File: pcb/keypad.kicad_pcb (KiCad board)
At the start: 2 copper layers, 53 x 53 mm, 36 parts, among them SW1 KS33_SW_solder, SW2 KS33_SW_solder, SW3 KS33_SW_solder, SW4 KS33_SW_solder, SW5 KS33_SW_solder, SW6 KS33_SW_solder, SW7 KS33_SW_solder, SW8 KS33_SW_solder, SW9 KS33_SW_solder, U1 74AHCT1G125, U2 XIAO-ESP32-C6-DIP

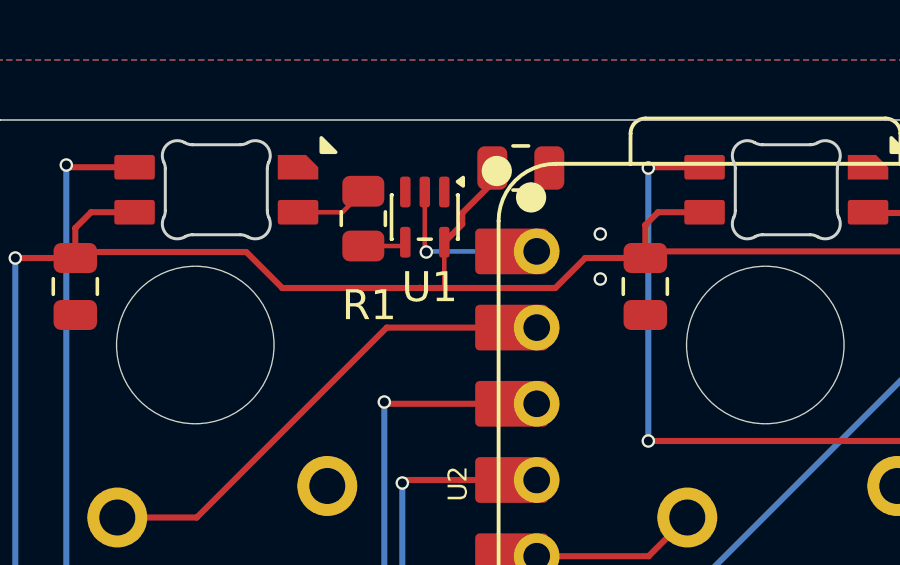
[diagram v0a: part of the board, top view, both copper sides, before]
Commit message: Swap U1 level shifter to SN74AHCT1G125DBVR (SOT-23-5)
The SOT-353 part was hard to hand solder. Same 74AHCT1G125 pinout, so only
the footprint changes. U1 shifts 0.1 mm right and its traces are rerouted;
gerbers regenerated.
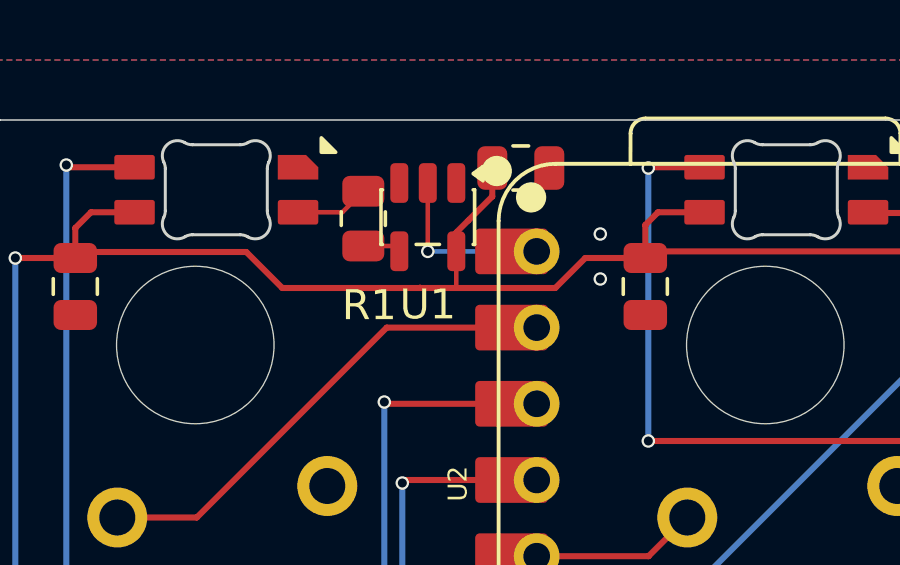
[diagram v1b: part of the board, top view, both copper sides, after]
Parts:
- U1: footprint Package_TO_SOT_SMD:SOT-353_SC-70-5 -> Package_TO_SOT_SMD:SOT-23-5
- moved U1 0.10 mm to (140.8, 78.7)

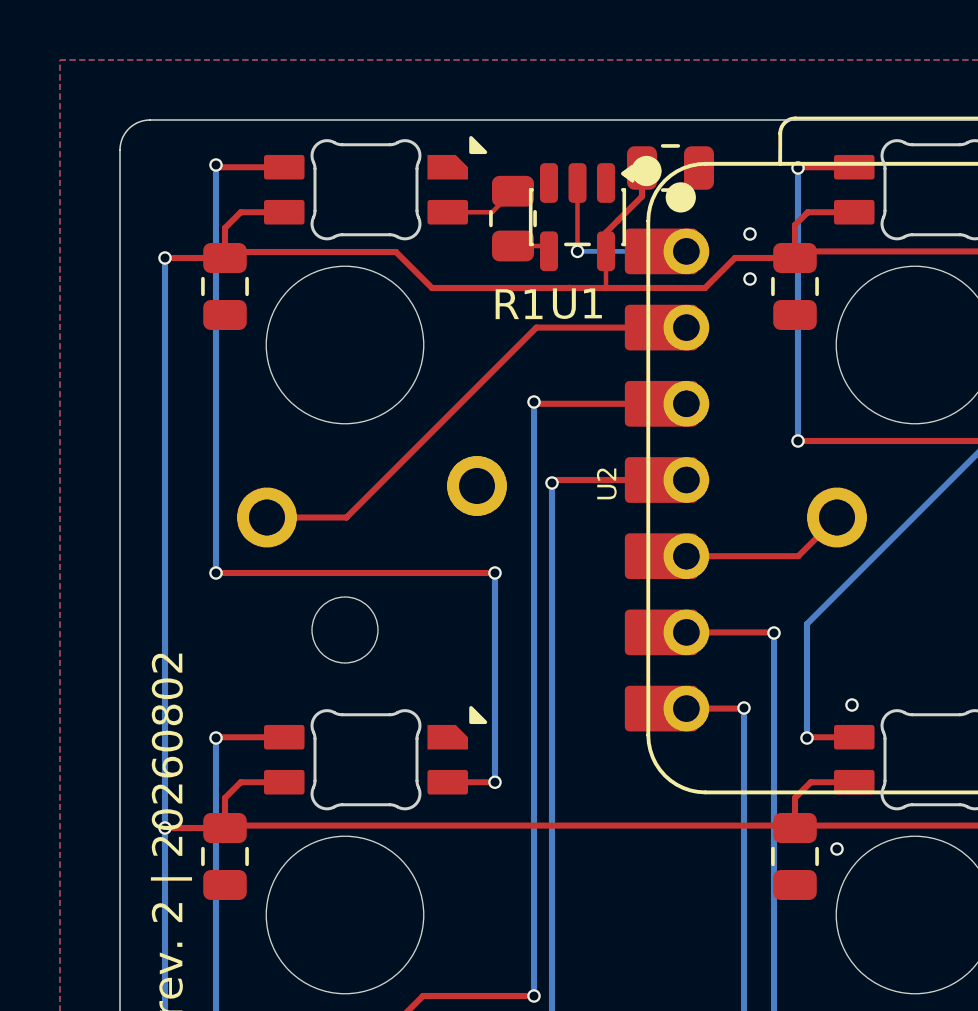
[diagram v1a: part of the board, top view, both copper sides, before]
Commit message: Rearrange U1 corner: move U1 and R1, reroute 5V and SW1 traces
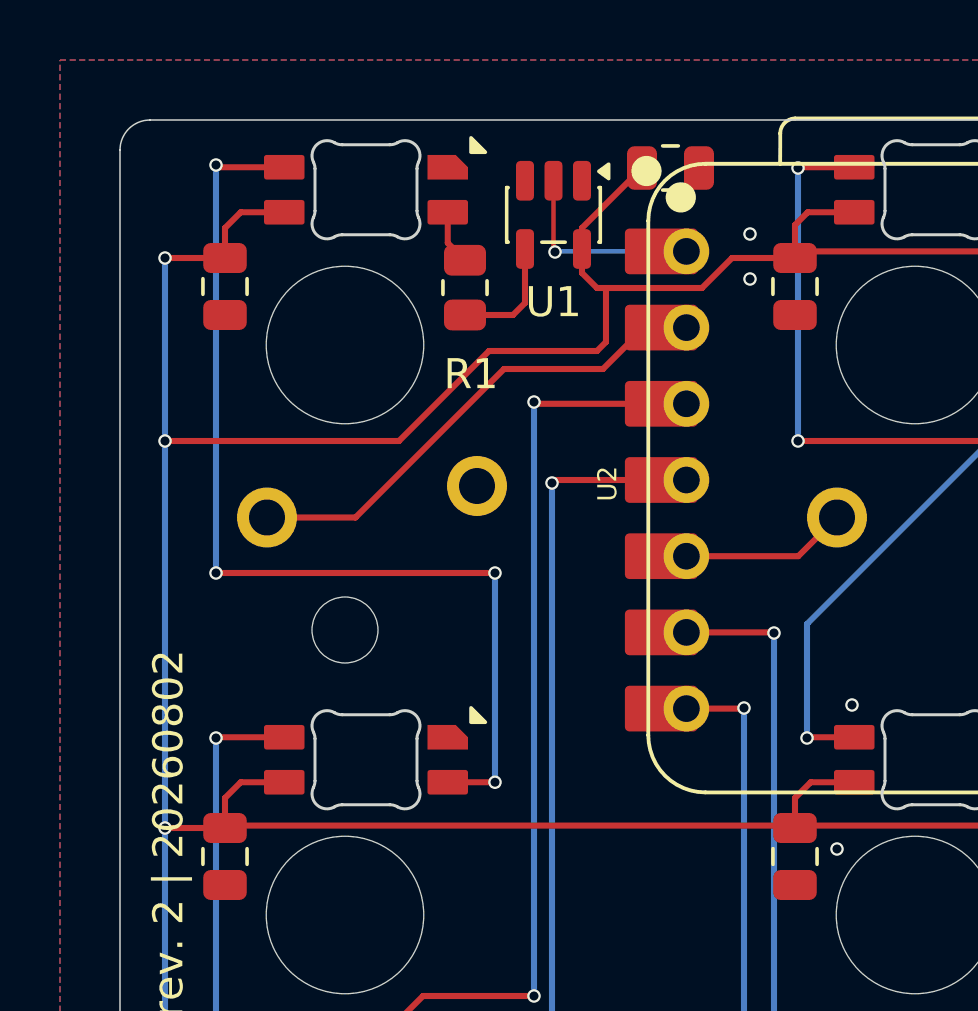
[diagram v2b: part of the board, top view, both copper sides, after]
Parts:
- moved R1 2.80 mm to (137.0, 81.1)
- moved U1 0.80 mm to (139.9, 78.7)
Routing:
- net +5V: track 192.5 -> 198.7 mm, vias 3 -> 4
- net /LED_D5.0: track 1.27 -> 3.97 mm
- net /LED_D3.3: track 6.73 -> 7.60 mm
- net /Switch Unit 1/DIN: track 2.46 -> 1.84 mm
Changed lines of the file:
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@@
 	(footprint "Resistor_SMD:R_0805_2012Metric"
 		(layer "F.Cu")
-		(at 138.6 78.7875 90)
+		(at 137 81.0875 90)
 		(descr "Resistor SMD 0805 (2012 Metric), square (rectangular) end terminal, IPC-7351 nominal, (Body size source: IPC-SM-782 page 72, https://www.pcb-3d.com/wordpress/wp-content/uploads/ipc-sm-782a_amendment_1_and_2.pdf)")
 		(tags "resistor")
@@
 	(footprint "Package_TO_SOT_SMD:SOT-23-5"
 		(layer "F.Cu")
-		(at 140.75 78.7375 -90)
+		(at 139.95 78.6625 -90)
 		(descr "SOT, 5 Pin (JEDEC MO-178 Var AA https://www.jedec.org/document_search?search_api_views_fulltext=MO-178)")
 		(tags "SOT TO_SOT_SMD")
@@
 	)
 	(segment
-		(start 140.75 77.6)
-		(end 140.75 79.88)
-		(width 0.152)
+		(start 139.95 79.85)
+		(end 139.95 77.525)
+		(width 0.1524)
+		(layer "F.Cu")
+		(net "/LED_D3.3")
+	)
+	(segment
+		(start 140 79.9)
+		(end 139.95 79.85)
+		(width 0.1524)
 		(layer "F.Cu")
 		(net "/LED_D3.3")
 	)
 	(via
-		(at 140.75 79.88)
+		(at 140 79.9)
 		(size 0.45)
 		(drill 0.3)
@@
 	)
 	(segment
+		(start 140.02 79.88)
+		(end 140 79.9)
+		(width 0.1524)
+		(layer "B.Cu")
+		(net "/LED_D3.3")
+	)
+	(segment
 		(start 144.38 79.88)
-		(end 140.75 79.88)
-		(width 0.152)
+		(end 140.02 79.88)
+		(width 0.1524)
 		(layer "B.Cu")
 		(net "/LED_D3.3")
@@
 	(segment
 		(start 144.38 82.42)
-		(end 139.38 82.42)
+		(end 142.98 82.42)
 		(width 0.2032)
 		(layer "F.Cu")
@@
 	)
 	(segment
-		(start 139.38 82.42)
-		(end 133.05 88.75)
+		(start 138.3 83.8)
+		(end 133.35 88.75)
 		(width 0.2032)
 		(layer "F.Cu")
@@
 	)
 	(segment
-		(start 133.05 88.75)
+		(start 133.35 88.75)
 		(end 130.4 88.75)
 		(width 0.2032)
@@
 	)
 	(segment
+		(start 142.98 82.42)
+		(end 141.6 83.8)
+		(width 0.2032)
+		(layer "F.Cu")
+		(net "/SW1")
+	)
+	(segment
+		(start 141.6 83.8)
+		(end 138.3 83.8)
+		(width 0.2032)
+		(layer "F.Cu")
+		(net "/SW1")
+	)
+	(segment
 		(start 139.3 104.7)
 		(end 135.6 104.7)
@@
 	)
 	(segment
+		(start 141.7 81.1)
+		(end 141.7 82.9)
+		(width 0.2032)
+		(layer "F.Cu")
+		(net "+5V")
+	)
+	(segment
 		(start 148 118.1)
 		(end 147.9194 118.0194)
@@
 	)
 	(segment
-		(start 140.4875 81.0875)
-		(end 140.5 81.1)
-		(width 0.2032)
-		(layer "F.Cu")
-		(net "+5V")
-	)
-	(segment
 		(start 129 99.1)
 		(end 127 99.1)
@@
 	)
 	(segment
-		(start 135.9 81.1)
-		(end 134.7 79.9)
+		(start 164 78.575)
+		(end 161.76 78.575)
 		(width 0.2032)
 		(layer "F.Cu")
@@
 	)
 	(segment
-		(start 164 78.575)
-		(end 161.76 78.575)
+		(start 137.8 83.2)
+		(end 134.8 86.2)
 		(width 0.2032)
 		(layer "F.Cu")
@@
 	)
 	(segment
-		(start 141.7 79.875)
-		(end 141.7 81.1)
-		(width 0.152)
-		(layer "F.Cu")
-		(net "+5V")
-	)
-	(segment
-		(start 141.7 79.25)
-		(end 142.1 78.85)
-		(width 0.203)
+		(start 129.425 116.575)
+		(end 129 117)
+		(width 0.2032)
 		(layer "F.Cu")
 		(net "+5V")
 	)
 	(segment
-		(start 129.425 116.575)
-		(end 129 117)
+		(start 140.9 79.8)
+		(end 140.9 80.6)
 		(width 0.2032)
 		(layer "F.Cu")
@@
 	)
 	(segment
-		(start 141.7 79.875)
-		(end 141.7 79.25)
-		(width 0.203)
+		(start 141.7 82.9)
+		(end 141.4 83.2)
+		(width 0.2032)
 		(layer "F.Cu")
 		(net "+5V")
@@
 	)
 	(segment
-		(start 148 80.1)
-		(end 146 80.1)
+		(start 129.0806 118.0194)
+		(end 129 118.1)
 		(width 0.2032)
 		(layer "F.Cu")
@@
 	)
 	(segment
-		(start 129.0806 118.0194)
-		(end 129 118.1)
+		(start 134.8 86.2)
+		(end 127 86.2)
 		(width 0.2032)
 		(layer "F.Cu")
@@
 	)
 	(segment
-		(start 146 80.1)
-		(end 145 81.1)
-		(width 0.2032)
-		(layer "F.Cu")
-		(net "+5V")
-	)
-	(segment
-		(start 141.3 81.1)
-		(end 140.5 81.1)
-		(width 0.2032)
-		(layer "F.Cu")
-		(net "+5V")
-	)
-	(segment
 		(start 148.425 116.575)
 		(end 148 117)
@@
 	)
 	(segment
-		(start 140.5 81.1)
-		(end 135.9 81.1)
+		(start 140.9 79.1)
+		(end 140.9 79.8)
 		(width 0.2032)
 		(layer "F.Cu")
@@
 	)
 	(segment
+		(start 148 80.1)
+		(end 145.9 80.1)
+		(width 0.2032)
+		(layer "F.Cu")
+		(net "+5V")
+	)
+	(segment
 		(start 168.975 78.575)
 		(end 167 78.575)
@@
 	)
 	(segment
+		(start 142.9 77.1)
+		(end 140.9 79.1)
+		(width 0.2032)
+		(layer "F.Cu")
+		(net "+5V")
+	)
+	(segment
 		(start 167 98.1)
 		(end 167 99.1)
@@
 	)
 	(segment
-		(start 142.9 78.05)
-		(end 142.9 77.6)
-		(width 0.203)
+		(start 140.9 80.6)
+		(end 141.4 81.1)
+		(width 0.2032)
 		(layer "F.Cu")
 		(net "+5V")
 	)
 	(segment
-		(start 145 81.1)
-		(end 141.3 81.1)
+		(start 144.9 81.1)
+		(end 141.7 81.1)
 		(width 0.2032)
 		(layer "F.Cu")
@@
 	)
 	(segment
-		(start 142.1 78.85)
-		(end 142.9 78.05)
-		(width 0.203)
+		(start 145.9 80.1)
+		(end 144.9 81.1)
+		(width 0.2032)
 		(layer "F.Cu")
 		(net "+5V")
@@
 	)
 	(segment
-		(start 149.975 78.575)
-		(end 148.425 78.575)
+		(start 141.4 81.1)
+		(end 141.7 81.1)
 		(width 0.2032)
 		(layer "F.Cu")
@@
 	)
 	(segment
-		(start 134.7 79.9)
-		(end 129.2 79.9)
+		(start 141.4 83.2)
+		(end 137.8 83.2)
+		(width 0.2032)
+		(layer "F.Cu")
+		(net "+5V")
+	)
+	(segment
+		(start 149.975 78.575)
+		(end 148.425 78.575)
 		(width 0.2032)
 		(layer "F.Cu")
@@
 		(net "+5V")
 	)
+	(via
+		(at 127 86.2)
+		(size 0.45)
+		(drill 0.3)
+		(layers "F.Cu" "B.Cu")
+		(net "+5V")
+	)
 	(segment
-		(start 127 80.1)
+		(start 127 86.2)
 		(end 127 99.1)
 		(width 0.2032)
@@
 	)
 	(segment
+		(start 127 80.1)
+		(end 127 86.2)
+		(width 0.2032)
+		(layer "B.Cu")
+		(net "+5V")
+	)
+	(segment
 		(start 127 99.1)
 		(end 127 118.1)
@@
 	(segment
 		(start 136.425 78.575)
-		(end 137.9 78.575)
-		(width 0.1524)
+		(end 136.425 79.6)
+		(width 0.2032)
 		(layer "F.Cu")
 		(net "/Switch Unit 1/DIN")
 	)
 	(segment
-		(start 137.9 78.575)
-		(end 138.6 77.875)
-		(width 0.1524)
+		(start 136.425 79.6)
+		(end 137 80.175)
+		(width 0.2032)
 		(layer "F.Cu")
 		(net "/Switch Unit 1/DIN")
@@
 	)
 	(segment
-		(start 138.6 79.7)
-		(end 139.625 79.7)
-		(width 0.152)
+		(start 138.6 82)
+		(end 137 82)
+		(width 0.2032)
 		(layer "F.Cu")
 		(net "/LED_D5.0")
 	)
 	(segment
-		(start 139.625 79.7)
-		(end 139.8 79.875)
-		(width 0.152)
+		(start 139 79.8)
+		(end 139 81.6)
+		(width 0.2032)
+		(layer "F.Cu")
+		(net "/LED_D5.0")
+	)
+	(segment
+		(start 139 81.6)
+		(end 138.6 82)
+		(width 0.2032)
 		(layer "F.Cu")
 		(net "/LED_D5.0")

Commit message: Use hand-soldering SOT-23-5 footprint for U1
Longer pads (1.56 x 0.65 mm) for easier hand soldering. Same position, pinout and routing; DRC unchanged.
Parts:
- U1: footprint Package_TO_SOT_SMD:SOT-23-5 -> Package_TO_SOT_SMD:SOT-23-5_HandSoldering
